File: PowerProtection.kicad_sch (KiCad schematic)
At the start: 10 parts, among them Q1 PMV35EPER, Q2 PMV35EPER

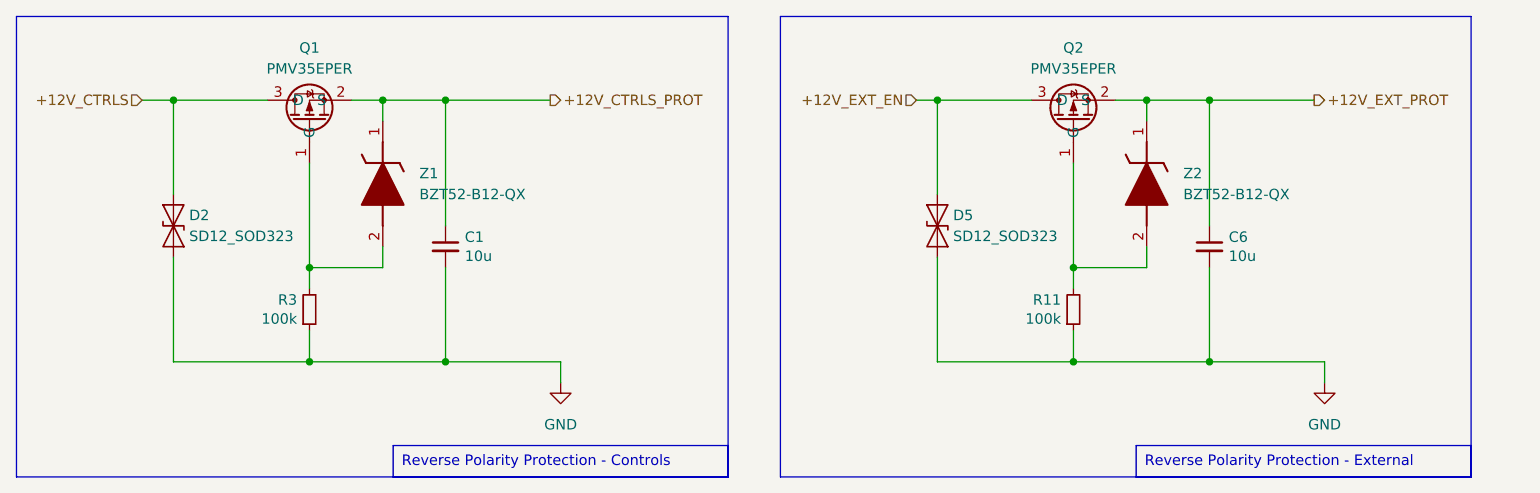
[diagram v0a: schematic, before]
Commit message: modify for PEAK candapter
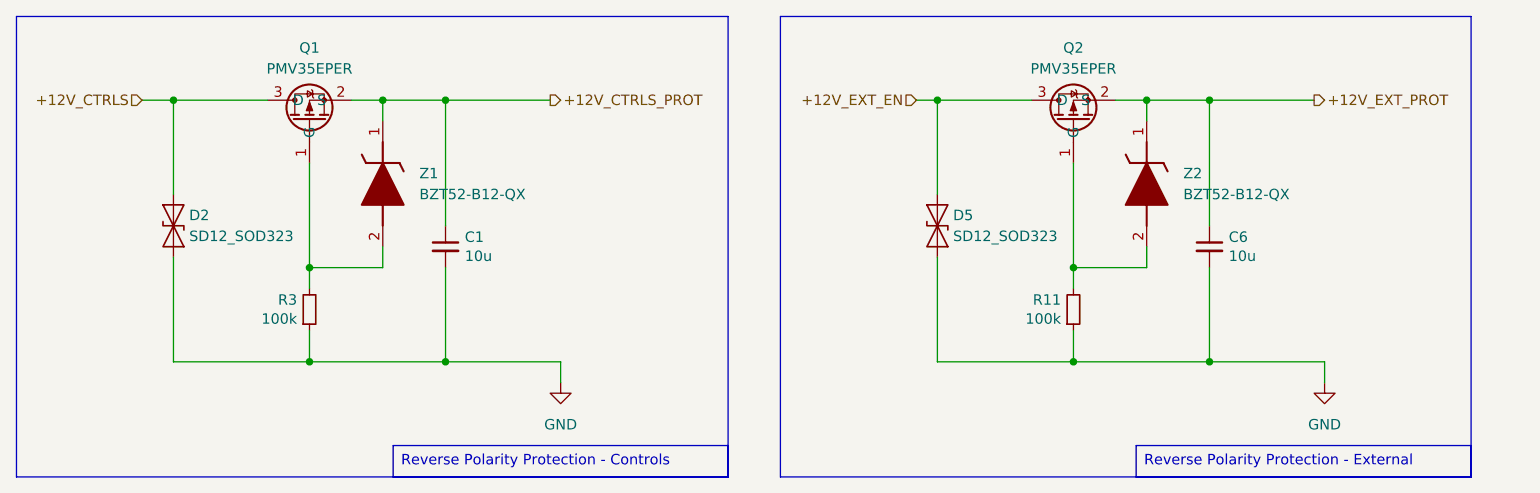
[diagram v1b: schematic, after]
